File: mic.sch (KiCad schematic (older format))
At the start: 8 parts, among them J6 JACK_TRS_5PINS

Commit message: Correct footprints for caps and DB15s
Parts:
- C2, C3, C4, C5, C6: footprint Capacitors_THT:C_Disc_D5.0mm_W2.5mm_P2.50mm -> blubaru:C_Disc_D5.5mm_W2.5mm_P2.50mm
- R1, R2: footprint Resistors_THT:R_Axial_DIN0204_L3.6mm_D1.6mm_P5.08mm_Horizontal -> Resistors_THT:R_Axial_DIN0204_L3.6mm_D1.6mm_P1.90mm_Vertical
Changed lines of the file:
@@
 F 0 "C5" H 5525 3850 50  0000 L CNN
 F 1 "47nF" H 5525 3650 50  0000 L CNN
-F 2 "Capacitors_THT:C_Disc_D5.0mm_W2.5mm_P2.50mm" H 5538 3600 50  0001 C CNN
-F 3 "" H 5500 3750 50  0000 C CNN
+F 2 "blubaru:C_Disc_D5.5mm_W2.5mm_P2.50mm" H 5538 3600 50  0001 C CNN
+F 3 "https://product.tdk.com/info/en/documents/spec/leadmlccspec_conventional_en.pdf" H 5500 3750 50  0001 C CNN
 	1    5500 3750
 	0    1    1    0
@@
 F 0 "C4" H 5175 4200 50  0000 L CNN
 F 1 "47nF" H 5175 4000 50  0000 L CNN
-F 2 "Capacitors_THT:C_Disc_D5.0mm_W2.5mm_P2.50mm" H 5188 3950 50  0001 C CNN
-F 3 "" H 5150 4100 50  0000 C CNN
+F 2 "blubaru:C_Disc_D5.5mm_W2.5mm_P2.50mm" H 5188 3950 50  0001 C CNN
+F 3 "https://product.tdk.com/info/en/documents/spec/leadmlccspec_conventional_en.pdf" H 5150 4100 50  0001 C CNN
 	1    5150 4100
 	1    0    0    -1
@@
 F 0 "C6" H 5525 4200 50  0000 L CNN
 F 1 "47nF" H 5525 4000 50  0000 L CNN
-F 2 "Capacitors_THT:C_Disc_D5.0mm_W2.5mm_P2.50mm" H 5538 3950 50  0001 C CNN
-F 3 "" H 5500 4100 50  0000 C CNN
+F 2 "blubaru:C_Disc_D5.5mm_W2.5mm_P2.50mm" H 5538 3950 50  0001 C CNN
+F 3 "https://product.tdk.com/info/en/documents/spec/leadmlccspec_conventional_en.pdf" H 5500 4100 50  0001 C CNN
 	1    5500 4100
 	1    0    0    -1
@@
 F 0 "C2" H 4925 4600 50  0000 L CNN
 F 1 "1uF" H 4925 4400 50  0000 L CNN
-F 2 "Capacitors_THT:C_Disc_D5.0mm_W2.5mm_P2.50mm" H 4938 4350 50  0001 C CNN
-F 3 "" H 4900 4500 50  0000 C CNN
+F 2 "blubaru:C_Disc_D5.5mm_W2.5mm_P2.50mm" H 4938 4350 50  0001 C CNN
+F 3 "https://product.tdk.com/info/en/documents/spec/leadmlccspec_conventional_en.pdf" H 4900 4500 50  0001 C CNN
 	1    4900 4500
 	1    0    0    -1
@@
 F 0 "C3" H 5175 3750 50  0000 L CNN
 F 1 "47nF" H 5175 3550 50  0000 L CNN
-F 2 "Capacitors_THT:C_Disc_D5.0mm_W2.5mm_P2.50mm" H 5188 3500 50  0001 C CNN
-F 3 "" H 5150 3650 50  0000 C CNN
+F 2 "blubaru:C_Disc_D5.5mm_W2.5mm_P2.50mm" H 5188 3500 50  0001 C CNN
+F 3 "https://product.tdk.com/info/en/documents/spec/leadmlccspec_conventional_en.pdf" H 5150 3650 50  0001 C CNN
 	1    5150 3650
 	0    1    1    0
@@
 F 0 "R1" V 5830 4000 50  0000 C CNN
 F 1 "2k2" V 5750 4000 50  0000 C CNN
-F 2 "Resistors_THT:R_Axial_DIN0204_L3.6mm_D1.6mm_P5.08mm_Horizontal" V 5680 4000 50  0001 C CNN
-F 3 "" H 5750 4000 50  0000 C CNN
+F 2 "Resistors_THT:R_Axial_DIN0204_L3.6mm_D1.6mm_P1.90mm_Vertical" V 5680 4000 50  0001 C CNN
+F 3 "https://www.seielect.com/Catalog/SEI-RNF_RNMF.pdf" H 5750 4000 50  0001 C CNN
 	1    5750 4000
 	1    0    0    -1
@@
 F 0 "R2" V 6030 3950 50  0000 C CNN
 F 1 "2k2" V 5950 3950 50  0000 C CNN
-F 2 "Resistors_THT:R_Axial_DIN0204_L3.6mm_D1.6mm_P5.08mm_Horizontal" V 5880 3950 50  0001 C CNN
-F 3 "" H 5950 3950 50  0000 C CNN
+F 2 "Resistors_THT:R_Axial_DIN0204_L3.6mm_D1.6mm_P1.90mm_Vertical" V 5880 3950 50  0001 C CNN
+F 3 "https://www.seielect.com/Catalog/SEI-RNF_RNMF.pdf" H 5950 3950 50  0001 C CNN
 	1    5950 3950
 	1    0    0    -1

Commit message: Add a line_driver schematic
This branch contains the full line driver with 2nd order filter, which
provides a low-pass filter on the input.
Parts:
- renumbered R1 to R2, R2 to R3
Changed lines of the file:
@@
 $EndComp
 $Comp
-L R R1
+L R R2
 U 1 1 589D2492
 P 5750 4000
-F 0 "R1" V 5830 4000 50  0000 C CNN
+F 0 "R2" V 5830 4000 50  0000 C CNN
 F 1 "2k2" V 5750 4000 50  0000 C CNN
 F 2 "Resistors_THT:R_Axial_DIN0204_L3.6mm_D1.6mm_P1.90mm_Vertical" V 5680 4000 50  0001 C CNN
@@
 $EndComp
 $Comp
-L R R2
+L R R3
 U 1 1 589D2525
 P 5950 3950
-F 0 "R2" V 6030 3950 50  0000 C CNN
+F 0 "R3" V 6030 3950 50  0000 C CNN
 F 1 "2k2" V 5950 3950 50  0000 C CNN
 F 2 "Resistors_THT:R_Axial_DIN0204_L3.6mm_D1.6mm_P1.90mm_Vertical" V 5880 3950 50  0001 C CNN
@@
 $EndComp
 $Comp
-L GND #PWR020
+L GND #PWR021
 U 1 1 589D259B
 P 4900 4750
-F 0 "#PWR020" H 4900 4500 50  0001 C CNN
+F 0 "#PWR021" H 4900 4500 50  0001 C CNN
 F 1 "GND" H 4900 4600 50  0000 C CNN
 F 2 "" H 4900 4750 50  0000 C CNN
@@
 $EndComp
 $Comp
-L GND #PWR021
+L GND #PWR022
 U 1 1 589E6671
 P 6250 4300
-F 0 "#PWR021" H 6250 4050 50  0001 C CNN
+F 0 "#PWR022" H 6250 4050 50  0001 C CNN
 F 1 "GND" H 6250 4150 50  0000 C CNN
 F 2 "" H 6250 4300 50  0000 C CNN

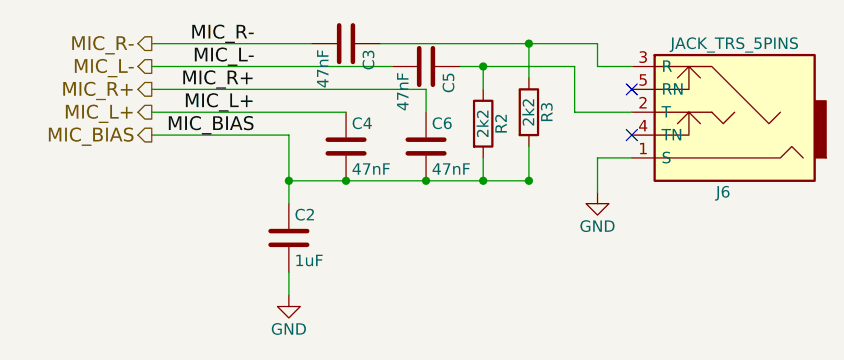
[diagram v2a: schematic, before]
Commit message: Adjust some cap prefixes and add large CD/Stereo labels to top level pages.
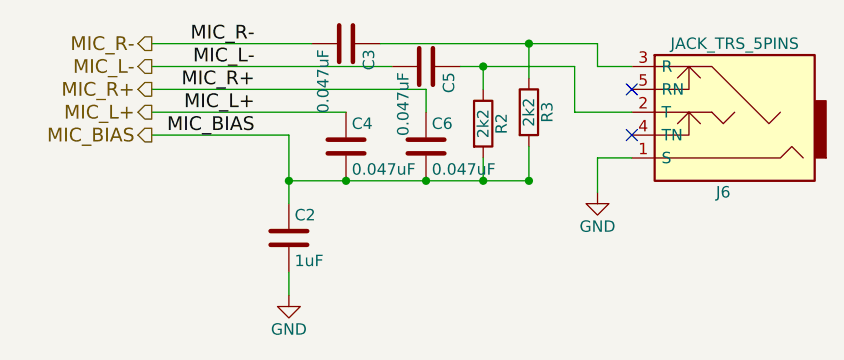
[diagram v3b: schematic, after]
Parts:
- C3, C4, C5, C6: value 47nF -> 0.047uF
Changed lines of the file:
@@
 P 5500 3750
 F 0 "C5" H 5525 3850 50  0000 L CNN
-F 1 "47nF" H 5525 3650 50  0000 L CNN
+F 1 "0.047uF" H 5525 3650 50  0000 L CNN
 F 2 "blubaru:C_Disc_D5.5mm_W2.5mm_P2.50mm" H 5538 3600 50  0001 C CNN
 F 3 "https://product.tdk.com/info/en/documents/spec/leadmlccspec_conventional_en.pdf" H 5500 3750 50  0001 C CNN
@@
 P 5150 4100
 F 0 "C4" H 5175 4200 50  0000 L CNN
-F 1 "47nF" H 5175 4000 50  0000 L CNN
+F 1 "0.047uF" H 5175 4000 50  0000 L CNN
 F 2 "blubaru:C_Disc_D5.5mm_W2.5mm_P2.50mm" H 5188 3950 50  0001 C CNN
 F 3 "https://product.tdk.com/info/en/documents/spec/leadmlccspec_conventional_en.pdf" H 5150 4100 50  0001 C CNN
@@
 P 5500 4100
 F 0 "C6" H 5525 4200 50  0000 L CNN
-F 1 "47nF" H 5525 4000 50  0000 L CNN
+F 1 "0.047uF" H 5525 4000 50  0000 L CNN
 F 2 "blubaru:C_Disc_D5.5mm_W2.5mm_P2.50mm" H 5538 3950 50  0001 C CNN
 F 3 "https://product.tdk.com/info/en/documents/spec/leadmlccspec_conventional_en.pdf" H 5500 4100 50  0001 C CNN
@@
 P 5150 3650
 F 0 "C3" H 5175 3750 50  0000 L CNN
-F 1 "47nF" H 5175 3550 50  0000 L CNN
+F 1 "0.047uF" H 5175 3550 50  0000 L CNN
 F 2 "blubaru:C_Disc_D5.5mm_W2.5mm_P2.50mm" H 5188 3500 50  0001 C CNN
 F 3 "https://product.tdk.com/info/en/documents/spec/leadmlccspec_conventional_en.pdf" H 5150 3650 50  0001 C CNN

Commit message: Add LEDs to MCU and polarized caps on line driver.
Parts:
- renumbered R2 to R5, R3 to R6
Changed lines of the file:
@@
 $EndComp
 $Comp
-L R R2
+L R R5
 U 1 1 589D2492
 P 5750 4000
-F 0 "R2" V 5830 4000 50  0000 C CNN
+F 0 "R5" V 5830 4000 50  0000 C CNN
 F 1 "2k2" V 5750 4000 50  0000 C CNN
 F 2 "Resistors_THT:R_Axial_DIN0204_L3.6mm_D1.6mm_P1.90mm_Vertical" V 5680 4000 50  0001 C CNN
@@
 $EndComp
 $Comp
-L R R3
+L R R6
 U 1 1 589D2525
 P 5950 3950
-F 0 "R3" V 6030 3950 50  0000 C CNN
+F 0 "R6" V 6030 3950 50  0000 C CNN
 F 1 "2k2" V 5950 3950 50  0000 C CNN
 F 2 "Resistors_THT:R_Axial_DIN0204_L3.6mm_D1.6mm_P1.90mm_Vertical" V 5880 3950 50  0001 C CNN
@@
 $EndComp
 $Comp
-L GND #PWR021
+L GND #PWR22
 U 1 1 589D259B
 P 4900 4750
-F 0 "#PWR021" H 4900 4500 50  0001 C CNN
+F 0 "#PWR22" H 4900 4500 50  0001 C CNN
 F 1 "GND" H 4900 4600 50  0000 C CNN
 F 2 "" H 4900 4750 50  0000 C CNN
@@
 $EndComp
 $Comp
-L GND #PWR022
+L GND #PWR23
 U 1 1 589E6671
 P 6250 4300
-F 0 "#PWR022" H 6250 4050 50  0001 C CNN
+F 0 "#PWR23" H 6250 4050 50  0001 C CNN
 F 1 "GND" H 6250 4150 50  0000 C CNN
 F 2 "" H 6250 4300 50  0000 C CNN

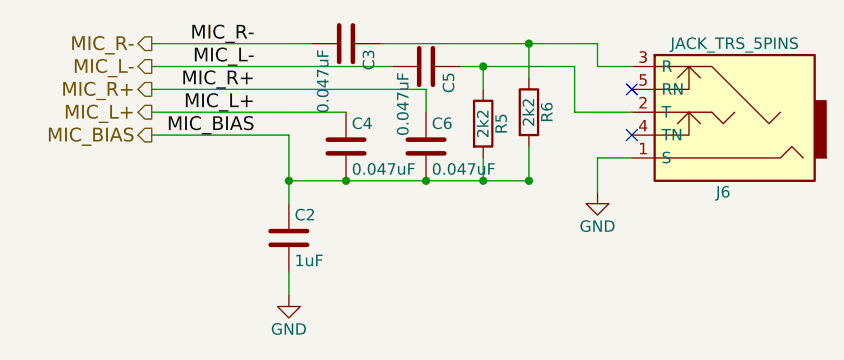
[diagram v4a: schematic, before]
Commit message: Add resistor values to LEDs and a voltage regulator. Has power pin errors still.
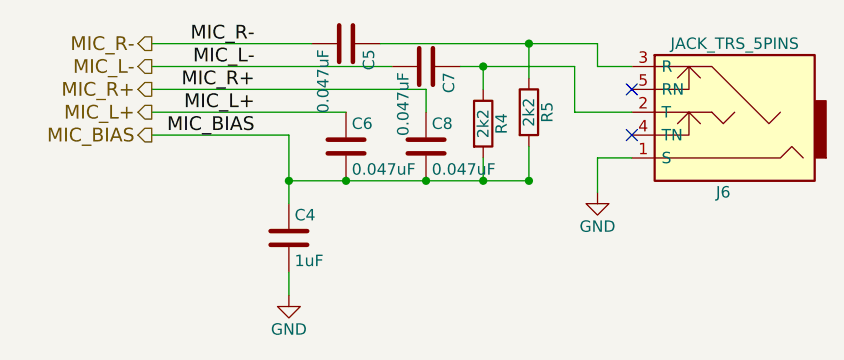
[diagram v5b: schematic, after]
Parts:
- renumbered C2 to C4, C3 to C5, C4 to C6, C5 to C7, C6 to C8, R5 to R4, R6 to R5
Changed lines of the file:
@@
 MIC_BIAS
 $Comp
-L C C5
+L C C7
 U 1 1 589D21D3
 P 5500 3750
-F 0 "C5" H 5525 3850 50  0000 L CNN
+F 0 "C7" H 5525 3850 50  0000 L CNN
 F 1 "0.047uF" H 5525 3650 50  0000 L CNN
 F 2 "blubaru:C_Disc_D5.5mm_W2.5mm_P2.50mm" H 5538 3600 50  0001 C CNN
@@
 $EndComp
 $Comp
-L C C4
+L C C6
 U 1 1 589D223D
 P 5150 4100
-F 0 "C4" H 5175 4200 50  0000 L CNN
+F 0 "C6" H 5175 4200 50  0000 L CNN
 F 1 "0.047uF" H 5175 4000 50  0000 L CNN
 F 2 "blubaru:C_Disc_D5.5mm_W2.5mm_P2.50mm" H 5188 3950 50  0001 C CNN
@@
 $EndComp
 $Comp
-L C C6
+L C C8
 U 1 1 589D230D
 P 5500 4100
-F 0 "C6" H 5525 4200 50  0000 L CNN
+F 0 "C8" H 5525 4200 50  0000 L CNN
 F 1 "0.047uF" H 5525 4000 50  0000 L CNN
 F 2 "blubaru:C_Disc_D5.5mm_W2.5mm_P2.50mm" H 5538 3950 50  0001 C CNN
@@
 $EndComp
 $Comp
-L C C2
+L C C4
 U 1 1 589D2382
 P 4900 4500
-F 0 "C2" H 4925 4600 50  0000 L CNN
+F 0 "C4" H 4925 4600 50  0000 L CNN
 F 1 "1uF" H 4925 4400 50  0000 L CNN
 F 2 "blubaru:C_Disc_D5.5mm_W2.5mm_P2.50mm" H 4938 4350 50  0001 C CNN
@@
 $EndComp
 $Comp
-L C C3
+L C C5
 U 1 1 589D23FA
 P 5150 3650
-F 0 "C3" H 5175 3750 50  0000 L CNN
+F 0 "C5" H 5175 3750 50  0000 L CNN
 F 1 "0.047uF" H 5175 3550 50  0000 L CNN
 F 2 "blubaru:C_Disc_D5.5mm_W2.5mm_P2.50mm" H 5188 3500 50  0001 C CNN
@@
 $EndComp
 $Comp
-L R R5
+L R R4
 U 1 1 589D2492
 P 5750 4000
-F 0 "R5" V 5830 4000 50  0000 C CNN
+F 0 "R4" V 5830 4000 50  0000 C CNN
 F 1 "2k2" V 5750 4000 50  0000 C CNN
 F 2 "Resistors_THT:R_Axial_DIN0204_L3.6mm_D1.6mm_P1.90mm_Vertical" V 5680 4000 50  0001 C CNN
@@
 $EndComp
 $Comp
-L R R6
+L R R5
 U 1 1 589D2525
 P 5950 3950
-F 0 "R6" V 6030 3950 50  0000 C CNN
+F 0 "R5" V 6030 3950 50  0000 C CNN
 F 1 "2k2" V 5950 3950 50  0000 C CNN
 F 2 "Resistors_THT:R_Axial_DIN0204_L3.6mm_D1.6mm_P1.90mm_Vertical" V 5880 3950 50  0001 C CNN
@@
 $EndComp
 $Comp
-L GND #PWR22
+L GND #PWR026
 U 1 1 589D259B
 P 4900 4750
-F 0 "#PWR22" H 4900 4500 50  0001 C CNN
+F 0 "#PWR026" H 4900 4500 50  0001 C CNN
 F 1 "GND" H 4900 4600 50  0000 C CNN
 F 2 "" H 4900 4750 50  0000 C CNN
@@
 $EndComp
 $Comp
-L GND #PWR23
+L GND #PWR027
 U 1 1 589E6671
 P 6250 4300
-F 0 "#PWR23" H 6250 4050 50  0001 C CNN
+F 0 "#PWR027" H 6250 4050 50  0001 C CNN
 F 1 "GND" H 6250 4150 50  0000 C CNN
 F 2 "" H 6250 4300 50  0000 C CNN

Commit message: Voltage regulator adjustments and tidying
Switch to LD1117 component and add decoupling caps.
Add a decoupling cap to the audio switch
Shift some status LEDs to modules layer
Use ProMini instead of ProMicro
Update BOM
Update netlist
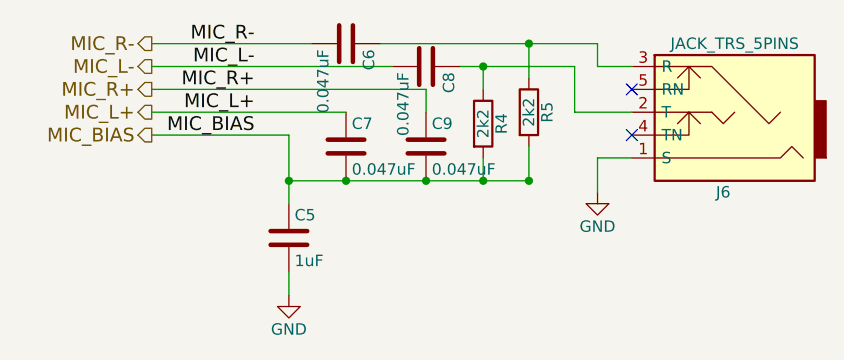
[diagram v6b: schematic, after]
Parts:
- renumbered C4 to C5, C5 to C6, C6 to C7, C7 to C8, C8 to C9
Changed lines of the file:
@@
 MIC_BIAS
 $Comp
-L C C7
+L C C8
 U 1 1 589D21D3
 P 5500 3750
-F 0 "C7" H 5525 3850 50  0000 L CNN
+F 0 "C8" H 5525 3850 50  0000 L CNN
 F 1 "0.047uF" H 5525 3650 50  0000 L CNN
 F 2 "blubaru:C_Disc_D5.5mm_W2.5mm_P2.50mm" H 5538 3600 50  0001 C CNN
@@
 $EndComp
 $Comp
-L C C6
+L C C7
 U 1 1 589D223D
 P 5150 4100
-F 0 "C6" H 5175 4200 50  0000 L CNN
+F 0 "C7" H 5175 4200 50  0000 L CNN
 F 1 "0.047uF" H 5175 4000 50  0000 L CNN
 F 2 "blubaru:C_Disc_D5.5mm_W2.5mm_P2.50mm" H 5188 3950 50  0001 C CNN
@@
 $EndComp
 $Comp
-L C C8
+L C C9
 U 1 1 589D230D
 P 5500 4100
-F 0 "C8" H 5525 4200 50  0000 L CNN
+F 0 "C9" H 5525 4200 50  0000 L CNN
 F 1 "0.047uF" H 5525 4000 50  0000 L CNN
 F 2 "blubaru:C_Disc_D5.5mm_W2.5mm_P2.50mm" H 5538 3950 50  0001 C CNN
@@
 $EndComp
 $Comp
-L C C4
+L C C5
 U 1 1 589D2382
 P 4900 4500
-F 0 "C4" H 4925 4600 50  0000 L CNN
+F 0 "C5" H 4925 4600 50  0000 L CNN
 F 1 "1uF" H 4925 4400 50  0000 L CNN
 F 2 "blubaru:C_Disc_D5.5mm_W2.5mm_P2.50mm" H 4938 4350 50  0001 C CNN
@@
 $EndComp
 $Comp
-L C C5
+L C C6
 U 1 1 589D23FA
 P 5150 3650
-F 0 "C5" H 5175 3750 50  0000 L CNN
+F 0 "C6" H 5175 3750 50  0000 L CNN
 F 1 "0.047uF" H 5175 3550 50  0000 L CNN
 F 2 "blubaru:C_Disc_D5.5mm_W2.5mm_P2.50mm" H 5188 3500 50  0001 C CNN

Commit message: Add new capacitor footprints and associate them.
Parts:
- C5: footprint blubaru:C_Disc_D5.5mm_W2.5mm_P2.50mm -> blubaru:C_Disc_D5.0mm_W3.2mm_P2.50mm
- C6, C7, C8, C9: footprint blubaru:C_Disc_D5.5mm_W2.5mm_P2.50mm -> blubaru:C_Disc_D4.0mm_W2.6mm_P2.50mm
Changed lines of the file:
@@
 F 0 "C8" H 5525 3850 50  0000 L CNN
 F 1 "0.047uF" H 5525 3650 50  0000 L CNN
-F 2 "blubaru:C_Disc_D5.5mm_W2.5mm_P2.50mm" H 5538 3600 50  0001 C CNN
+F 2 "blubaru:C_Disc_D4.0mm_W2.6mm_P2.50mm" H 5538 3600 50  0001 C CNN
 F 3 "https://product.tdk.com/info/en/documents/spec/leadmlccspec_conventional_en.pdf" H 5500 3750 50  0001 C CNN
 	1    5500 3750
@@
 F 0 "C7" H 5175 4200 50  0000 L CNN
 F 1 "0.047uF" H 5175 4000 50  0000 L CNN
-F 2 "blubaru:C_Disc_D5.5mm_W2.5mm_P2.50mm" H 5188 3950 50  0001 C CNN
+F 2 "blubaru:C_Disc_D4.0mm_W2.6mm_P2.50mm" H 5188 3950 50  0001 C CNN
 F 3 "https://product.tdk.com/info/en/documents/spec/leadmlccspec_conventional_en.pdf" H 5150 4100 50  0001 C CNN
 	1    5150 4100
@@
 F 0 "C9" H 5525 4200 50  0000 L CNN
 F 1 "0.047uF" H 5525 4000 50  0000 L CNN
-F 2 "blubaru:C_Disc_D5.5mm_W2.5mm_P2.50mm" H 5538 3950 50  0001 C CNN
+F 2 "blubaru:C_Disc_D4.0mm_W2.6mm_P2.50mm" H 5538 3950 50  0001 C CNN
 F 3 "https://product.tdk.com/info/en/documents/spec/leadmlccspec_conventional_en.pdf" H 5500 4100 50  0001 C CNN
 	1    5500 4100
@@
 F 0 "C5" H 4925 4600 50  0000 L CNN
 F 1 "1uF" H 4925 4400 50  0000 L CNN
-F 2 "blubaru:C_Disc_D5.5mm_W2.5mm_P2.50mm" H 4938 4350 50  0001 C CNN
+F 2 "blubaru:C_Disc_D5.0mm_W3.2mm_P2.50mm" H 4938 4350 50  0001 C CNN
 F 3 "https://product.tdk.com/info/en/documents/spec/leadmlccspec_conventional_en.pdf" H 4900 4500 50  0001 C CNN
 	1    4900 4500
@@
 F 0 "C6" H 5175 3750 50  0000 L CNN
 F 1 "0.047uF" H 5175 3550 50  0000 L CNN
-F 2 "blubaru:C_Disc_D5.5mm_W2.5mm_P2.50mm" H 5188 3500 50  0001 C CNN
+F 2 "blubaru:C_Disc_D4.0mm_W2.6mm_P2.50mm" H 5188 3500 50  0001 C CNN
 F 3 "https://product.tdk.com/info/en/documents/spec/leadmlccspec_conventional_en.pdf" H 5150 3650 50  0001 C CNN
 	1    5150 3650
